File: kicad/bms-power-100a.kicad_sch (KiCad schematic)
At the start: 67 parts, among them J1 Conn_01x06, J2 Conn_01x06, P1 CONN_01X01, P2 CONN_01X01, P3 CONN_01X01, P4 CONN_01X01, Q1 IPT015N10N5, Q10 BSS123N, Q2 IPT015N10N5, Q21 ZXMP6A13F, Q3 IPT015N10N5, Q4 IPT015N10N5, Q5 IPT015N10N5, Q6 IPT015N10N5, Q7 IPT015N10N5, Q8 IPT015N10N5, Q9 DMG1013UW

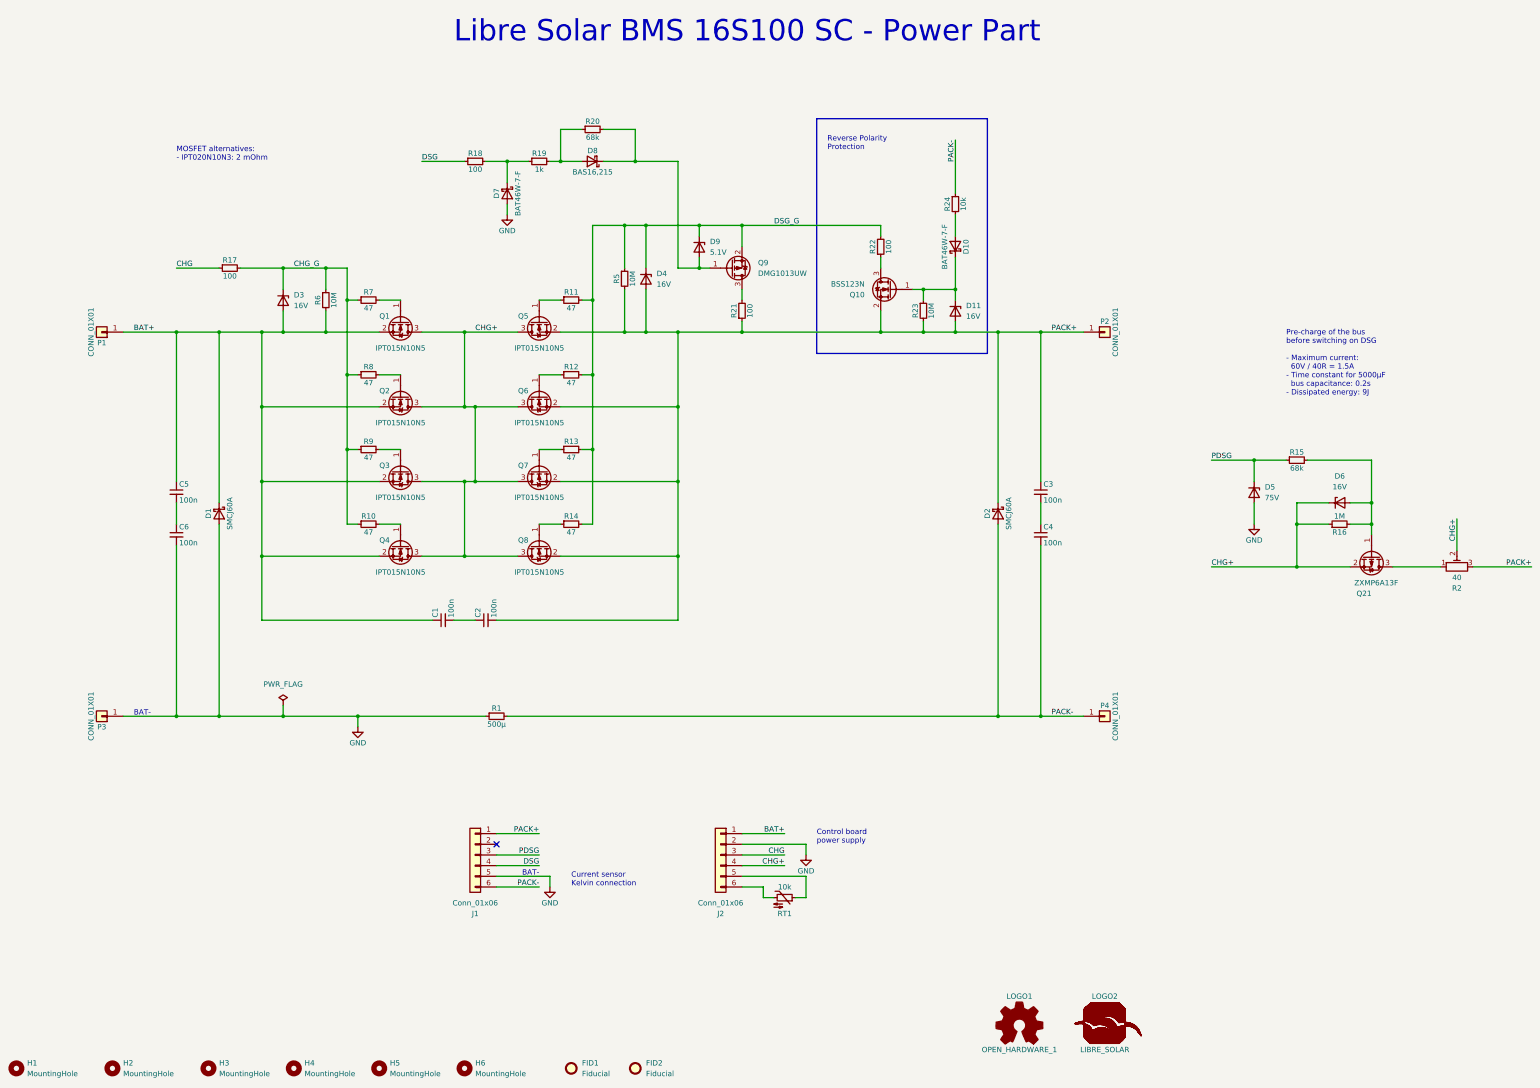
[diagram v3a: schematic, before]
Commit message: Updates based on review comments (v0.2)
This is the design revision that was ordered for the first prototype build.

The pinout of the cell connector and the board-to-board connector changed
compared to v0.1, hence it got a minor revision update.

The control board is now a 4-layer board to improve the grounding of the
PCB. Various other suggested improvements from the design review are also
included in this update.

Fixes #11, #12, #13, #17, #18, #19
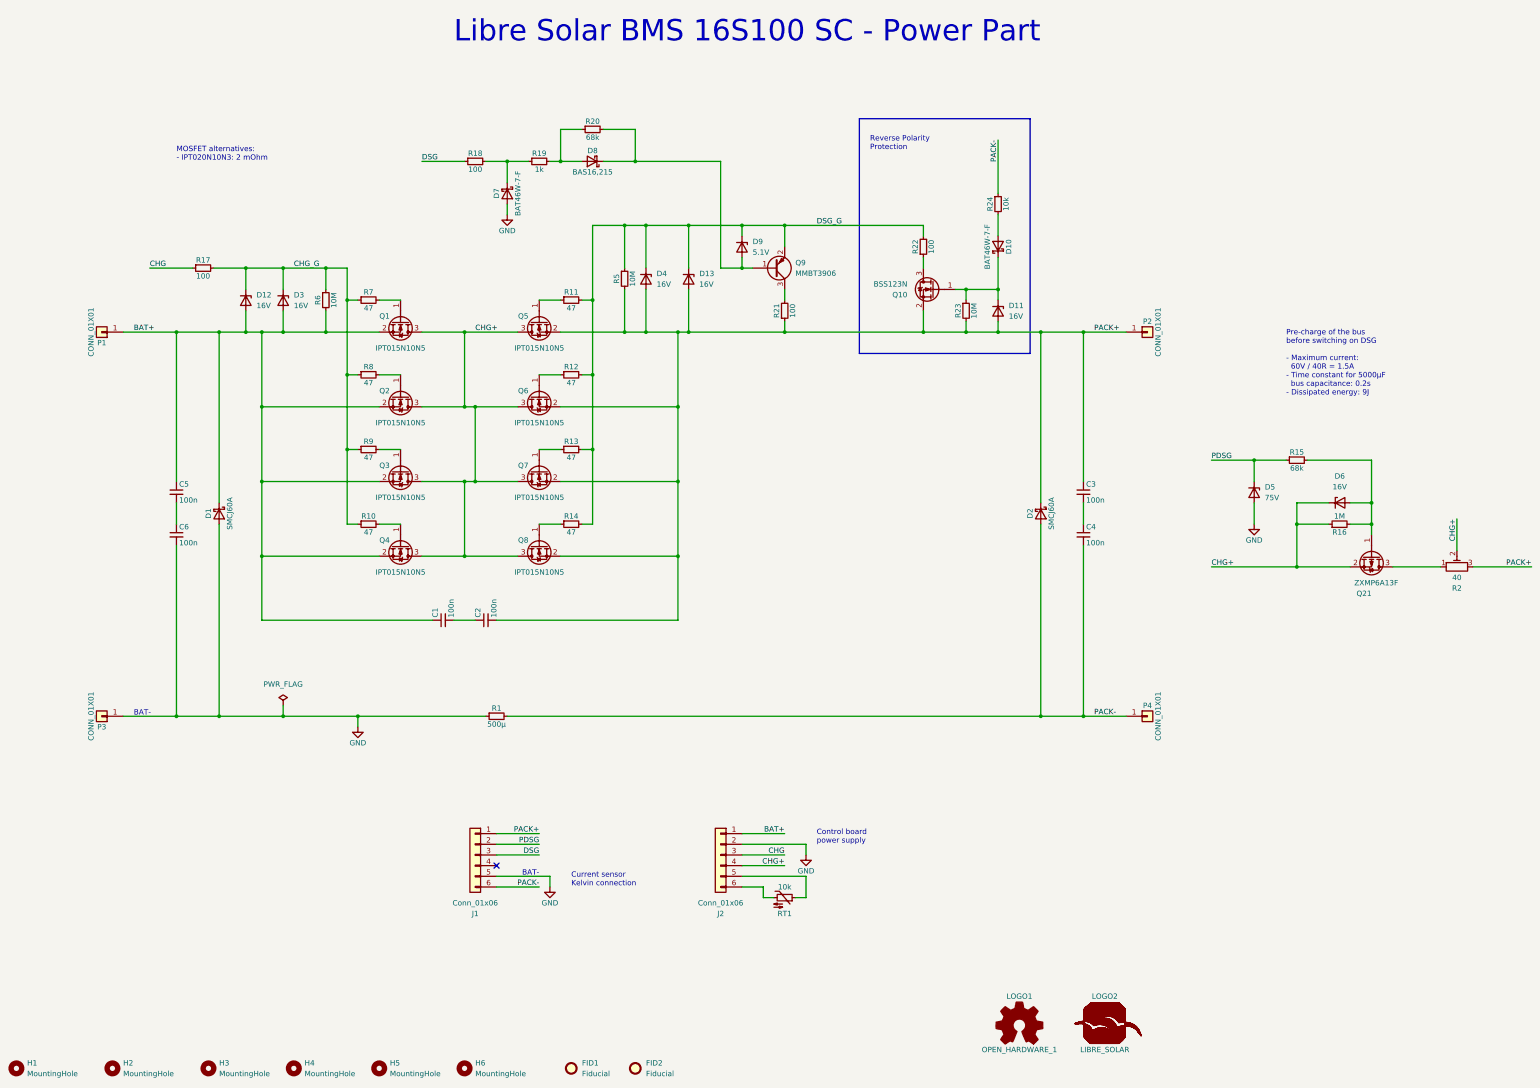
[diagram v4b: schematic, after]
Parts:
- removed Q9: DMG1013UW, Package_TO_SOT_SMD:SOT-323_SC-70, symbol Device:Q_PMOS_GSD
- added D12, D13: 16V, LibreSolar:D_SOD-123, symbol LibreSolar:D_Zener
- added Q9: MMBT3906, Package_TO_SOT_SMD:SOT-23, symbol Transistor_BJT:MMBT3906
- D10, D7: Remarks (none) -> Alternative: MCC BAT46WHE3-TP
- D11, D3, D4, D6: Remarks (none) -> Alternative: Vishay MMSZ5246B-HE3-08
- D9: Remarks (none) -> Vishay BZX384C5V1
- J1, J2: footprint Connector_PinHeader_2.00mm:PinHeader_1x06_P2.00mm_Vertical_SMD_Pin1Left -> LibreSolar:PinHeader_1x06_P2.00mm_Vertical_SMD
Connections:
- net BAT+: now also D12.2 (A)
- net CHG_G: now also D12.1 (K)
- net DSG: now also J1.3 (Pin_3); no longer J1.4 (Pin_4)
- net DSG_G: now also D13.1 (K), Q9.2 (E)
- net PACK+: now also D13.2 (A)
- net PDSG: now also J1.2 (Pin_2); no longer J1.3 (Pin_3)
- net at D8.1 (K), D9.2 (A), R20.2: now also Q9.1 (B)
- net at R21.2: now also Q9.3 (C)
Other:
- moved on the sheet: C3, C4, D10, D11, D2, D9, P2, P4, Q10, R17, R21, R22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
